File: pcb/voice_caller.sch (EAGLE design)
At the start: 44 parts, among them IC1 PRO_MICRO, IC2 LM386M-1, IC3 78L12SMD, K1 TQ2SA-L2-5V, U1 25F32006WSOI

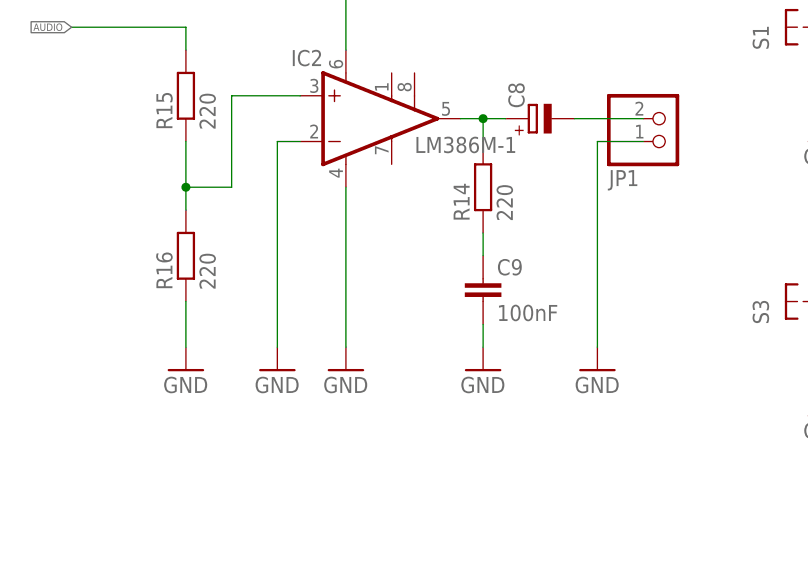
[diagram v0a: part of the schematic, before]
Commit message: Bypass capacitor added for LM386.
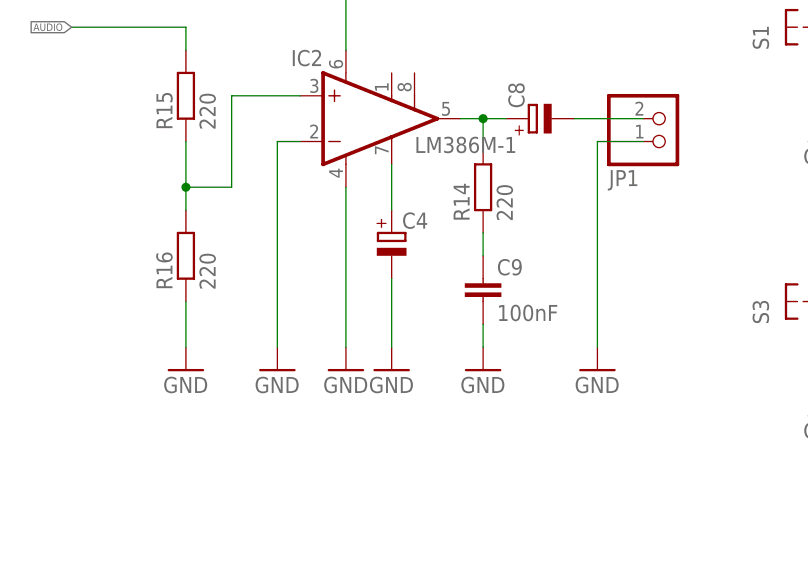
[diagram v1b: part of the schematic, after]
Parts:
- added C4: (no value), rcl:CPOL-EUE2.5-6
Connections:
- new net N$7: C4.+, IC2.BYPASS
- net GND: now also C4.-
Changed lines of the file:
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@@
 <part name="R16" library="rcl" deviceset="R-EU_" device="M1206" value="220"/>
 <part name="C11" library="rcl" deviceset="CPOL-EU" device="E2.5-6"/>
+<part name="GND26" library="supply1" deviceset="GND" device=""/>
+<part name="C4" library="rcl" deviceset="CPOL-EU" device="E2.5-6"/>
 </parts>
 <sheets>
@@
 <instance part="R16" gate="G$1" x="-91.44" y="104.14" rot="R90"/>
 <instance part="C11" gate="G$1" x="73.66" y="109.22" rot="R90"/>
+<instance part="GND26" gate="1" x="-68.58" y="91.44"/>
+<instance part="C4" gate="G$1" x="-68.58" y="106.68"/>
 </instances>
 <busses>
@@
 <pinref part="R16" gate="G$1" pin="1"/>
 </segment>
+<segment>
+<pinref part="GND26" gate="1" pin="GND"/>
+<pinref part="C4" gate="G$1" pin="-"/>
+<wire x1="-68.58" y1="93.98" x2="-68.58" y2="101.6" width="0.1524" layer="91"/>
+</segment>
 </net>
 <net name="MOSI" class="0">
@@
 </segment>
 </net>
+<net name="N$7" class="0">
+<segment>
+<pinref part="C4" gate="G$1" pin="+"/>
+<pinref part="IC2" gate="G$1" pin="BYPASS"/>
+<wire x1="-68.58" y1="109.22" x2="-68.58" y2="114.3" width="0.1524" layer="91"/>
+</segment>
+</net>

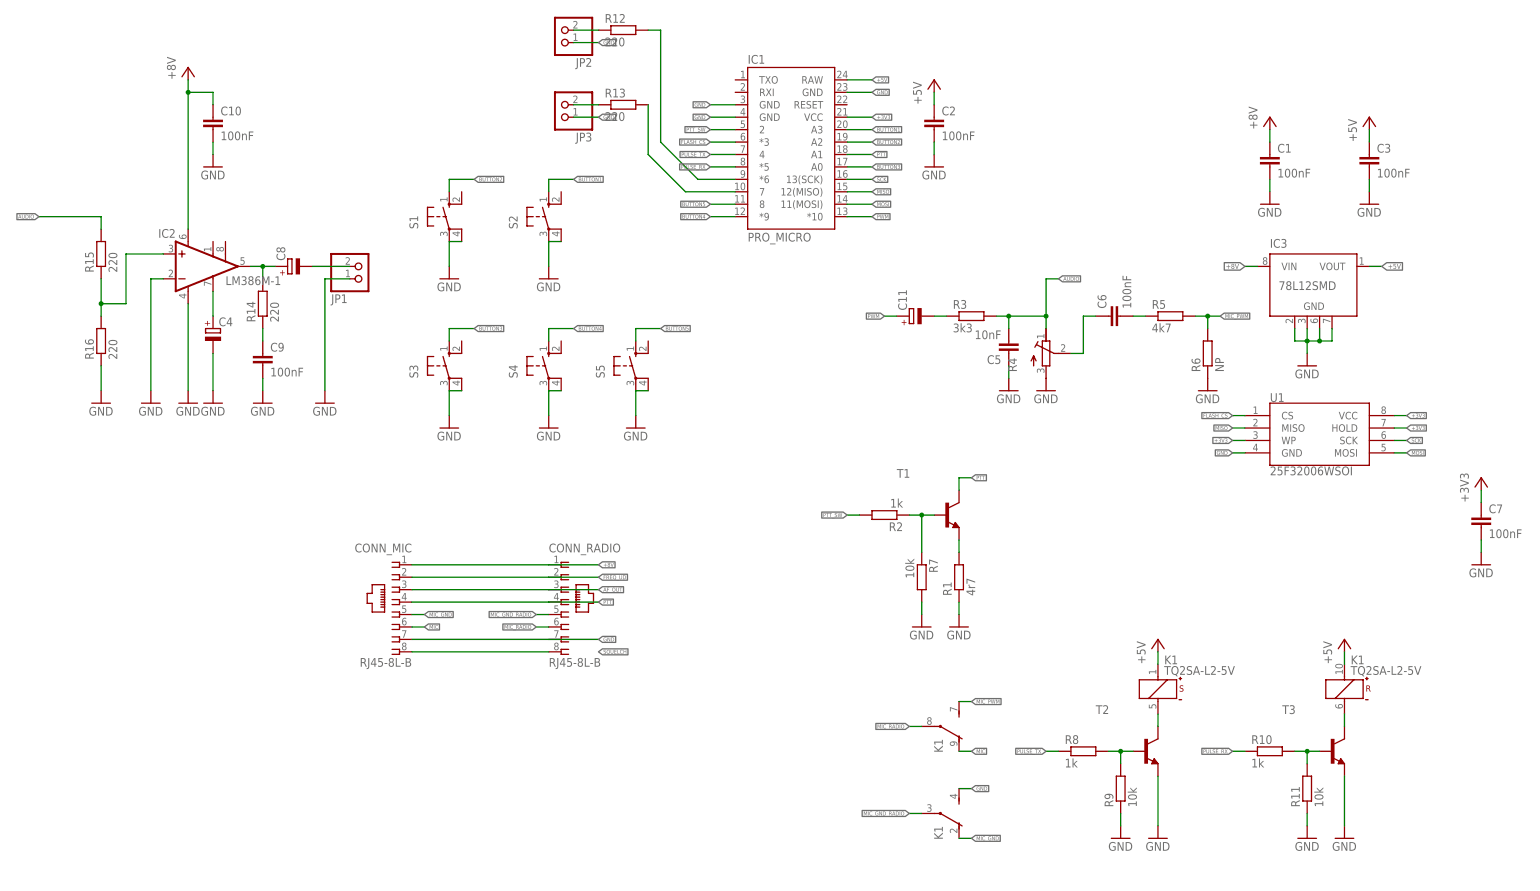
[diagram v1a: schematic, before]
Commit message: PTT sensing circuity added.
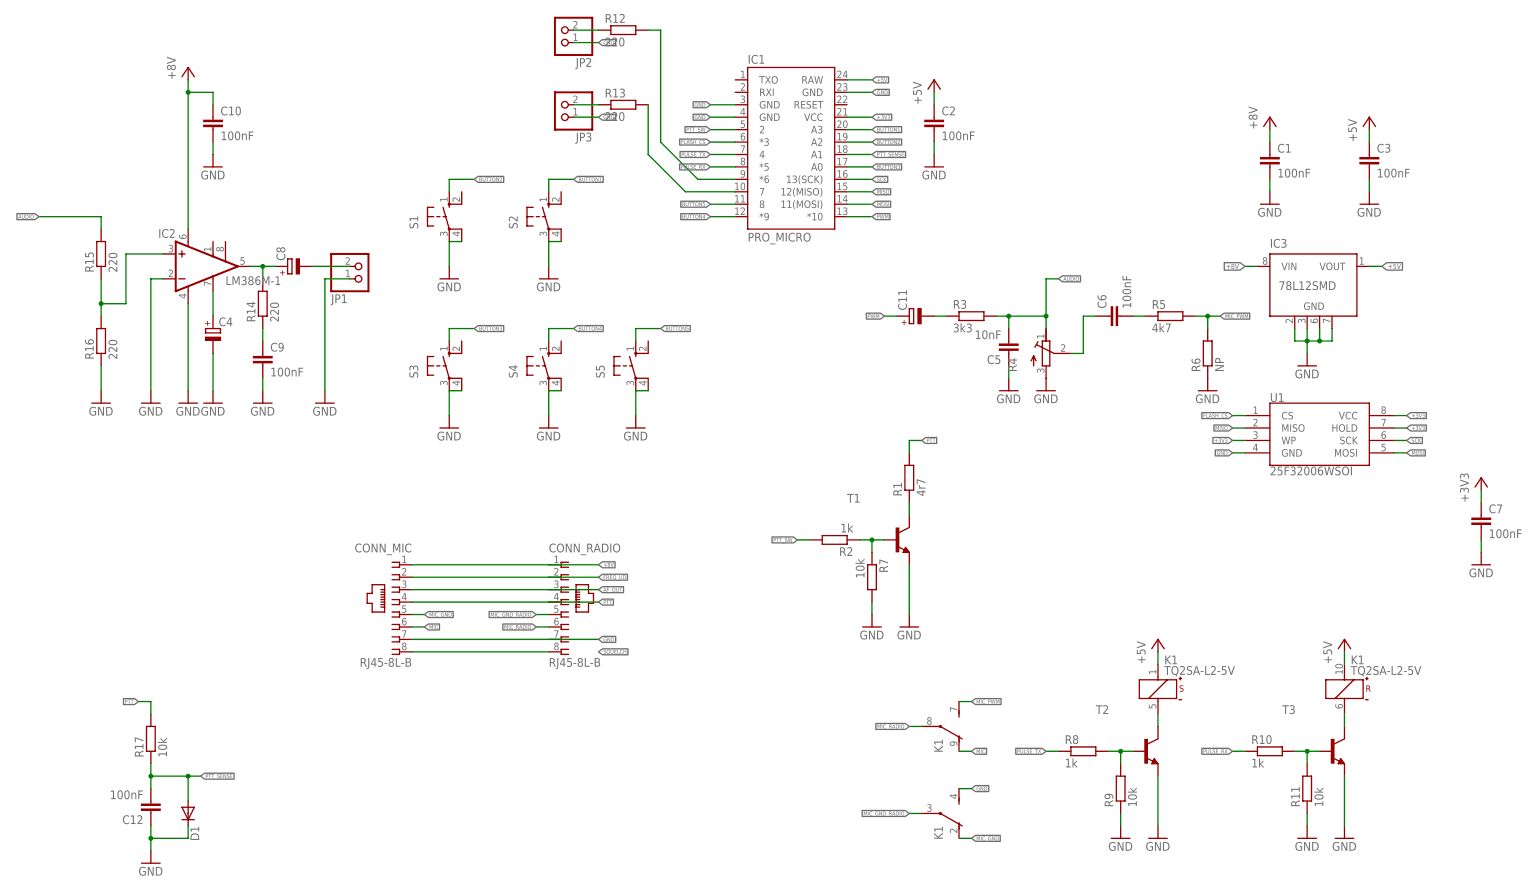
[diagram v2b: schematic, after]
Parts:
- added C12: 100nF, rcl:C-EUC1206K
- added D1: (no value), diode:DIODE-SOD80C
- added R17: 10k, rcl:R-EU_M1206
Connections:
- new net N$8: R1.1, T1.C
- net GND: now also C12.1, D1.C, T1.E; no longer R1.1
- net PTT: now also R1.2, R17.2; no longer IC1.A1, T1.C
- net PTT_SENSE: now also C12.2, D1.A, IC1.A1, R17.1; no longer R1.2, T1.E
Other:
- moved on the sheet: R1, R2, R7, T1
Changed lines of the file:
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@@
 <part name="GND26" library="supply1" deviceset="GND" device=""/>
 <part name="C4" library="rcl" deviceset="CPOL-EU" device="E2.5-6"/>
+<part name="R17" library="rcl" deviceset="R-EU_" device="M1206" value="10k"/>
+<part name="C12" library="rcl" deviceset="C-EU" device="C1206K" value="100nF"/>
+<part name="D1" library="diode" deviceset="DIODE-" device="SOD80C"/>
+<part name="GND27" library="supply1" deviceset="GND" device=""/>
 </parts>
 <sheets>
@@
 <instance part="S5" gate="1" x="17.78" y="99.06"/>
 <instance part="GND17" gate="1" x="17.78" y="86.36"/>
-<instance part="T1" gate="G$1" x="81.28" y="68.58"/>
-<instance part="R1" gate="G$1" x="83.82" y="55.88" rot="R90"/>
-<instance part="GND18" gate="1" x="83.82" y="45.72"/>
-<instance part="R2" gate="G$1" x="68.58" y="68.58" rot="R180"/>
-<instance part="R7" gate="G$1" x="76.2" y="55.88" rot="R270"/>
-<instance part="GND19" gate="1" x="76.2" y="45.72"/>
+<instance part="T1" gate="G$1" x="71.12" y="63.5"/>
+<instance part="R1" gate="G$1" x="73.66" y="76.2" rot="R90"/>
+<instance part="GND18" gate="1" x="73.66" y="45.72"/>
+<instance part="R2" gate="G$1" x="58.42" y="63.5" rot="R180"/>
+<instance part="R7" gate="G$1" x="66.04" y="55.88" rot="R270"/>
+<instance part="GND19" gate="1" x="66.04" y="45.72"/>
 <instance part="R12" gate="G$1" x="15.24" y="167.64"/>
 <instance part="R13" gate="G$1" x="15.24" y="152.4"/>
@@
 <instance part="GND26" gate="1" x="-68.58" y="91.44"/>
 <instance part="C4" gate="G$1" x="-68.58" y="106.68"/>
+<instance part="R17" gate="G$1" x="-81.28" y="22.86" rot="R90"/>
+<instance part="C12" gate="G$1" x="-81.28" y="7.62" rot="R180"/>
+<instance part="D1" gate="G$1" x="-73.66" y="7.62" rot="R270"/>
+<instance part="GND27" gate="1" x="-81.28" y="-2.54"/>
 </instances>
 <busses>
@@
 </segment>
 <segment>
-<pinref part="R1" gate="G$1" pin="1"/>
-<pinref part="GND18" gate="1" pin="GND"/>
-<wire x1="83.82" y1="48.26" x2="83.82" y2="50.8" width="0.1524" layer="91"/>
-</segment>
-<segment>
 <pinref part="R7" gate="G$1" pin="2"/>
 <pinref part="GND19" gate="1" pin="GND"/>
-<wire x1="76.2" y1="48.26" x2="76.2" y2="50.8" width="0.1524" layer="91"/>
+<wire x1="66.04" y1="48.26" x2="66.04" y2="50.8" width="0.1524" layer="91"/>
 </segment>
 <segment>
@@
 <pinref part="C4" gate="G$1" pin="-"/>
 <wire x1="-68.58" y1="93.98" x2="-68.58" y2="101.6" width="0.1524" layer="91"/>
+</segment>
+<segment>
+<pinref part="T1" gate="G$1" pin="E"/>
+<pinref part="GND18" gate="1" pin="GND"/>
+<wire x1="73.66" y1="58.42" x2="73.66" y2="48.26" width="0.1524" layer="91"/>
+</segment>
+<segment>
+<pinref part="C12" gate="G$1" pin="1"/>
+<wire x1="-81.28" y1="5.08" x2="-81.28" y2="2.54" width="0.1524" layer="91"/>
+<wire x1="-81.28" y1="2.54" x2="-73.66" y2="2.54" width="0.1524" layer="91"/>
+<pinref part="D1" gate="G$1" pin="C"/>
+<wire x1="-73.66" y1="2.54" x2="-73.66" y2="5.08" width="0.1524" layer="91"/>
+<pinref part="GND27" gate="1" pin="GND"/>
+<wire x1="-81.28" y1="0" x2="-81.28" y2="2.54" width="0.1524" layer="91"/>
+<junction x="-81.28" y="2.54"/>
 </segment>
 </net>
@@
 </segment>
 <segment>
-<pinref part="T1" gate="G$1" pin="C"/>
-<wire x1="83.82" y1="73.66" x2="83.82" y2="76.2" width="0.1524" layer="91"/>
-<wire x1="83.82" y1="76.2" x2="86.36" y2="76.2" width="0.1524" layer="91"/>
-<label x="86.36" y="76.2" size="0.8128" layer="95" xref="yes"/>
-</segment>
-<segment>
-<pinref part="IC1" gate="G$1" pin="A1"/>
-<wire x1="60.96" y1="142.24" x2="66.04" y2="142.24" width="0.1524" layer="91"/>
-<label x="66.04" y="142.24" size="0.8128" layer="95" xref="yes"/>
+<wire x1="73.66" y1="83.82" x2="76.2" y2="83.82" width="0.1524" layer="91"/>
+<label x="76.2" y="83.82" size="0.8128" layer="95" xref="yes"/>
+<pinref part="R1" gate="G$1" pin="2"/>
+<wire x1="73.66" y1="81.28" x2="73.66" y2="83.82" width="0.1524" layer="91"/>
+</segment>
+<segment>
+<pinref part="R17" gate="G$1" pin="2"/>
+<wire x1="-81.28" y1="27.94" x2="-81.28" y2="30.48" width="0.1524" layer="91"/>
+<wire x1="-81.28" y1="30.48" x2="-83.82" y2="30.48" width="0.1524" layer="91"/>
+<label x="-83.82" y="30.48" size="0.8128" layer="95" rot="R180" xref="yes"/>
 </segment>
 </net>
@@
 <net name="PTT_SENSE" class="0">
 <segment>
-<pinref part="T1" gate="G$1" pin="E"/>
-<pinref part="R1" gate="G$1" pin="2"/>
-<wire x1="83.82" y1="60.96" x2="83.82" y2="63.5" width="0.1524" layer="91"/>
+<pinref part="IC1" gate="G$1" pin="A1"/>
+<wire x1="60.96" y1="142.24" x2="66.04" y2="142.24" width="0.1524" layer="91"/>
+<label x="66.04" y="142.24" size="0.8128" layer="95" xref="yes"/>
+</segment>
+<segment>
+<pinref part="R17" gate="G$1" pin="1"/>
+<wire x1="-81.28" y1="17.78" x2="-81.28" y2="15.24" width="0.1524" layer="91"/>
+<pinref part="C12" gate="G$1" pin="2"/>
+<wire x1="-81.28" y1="15.24" x2="-81.28" y2="12.7" width="0.1524" layer="91"/>
+<wire x1="-81.28" y1="15.24" x2="-73.66" y2="15.24" width="0.1524" layer="91"/>
+<pinref part="D1" gate="G$1" pin="A"/>
+<wire x1="-73.66" y1="15.24" x2="-73.66" y2="10.16" width="0.1524" layer="91"/>
+<junction x="-81.28" y="15.24"/>
+<wire x1="-73.66" y1="15.24" x2="-71.12" y2="15.24" width="0.1524" layer="91"/>
+<junction x="-73.66" y="15.24"/>
+<label x="-71.12" y="15.24" size="0.8128" layer="95" xref="yes"/>
 </segment>
 </net>
@@
 <segment>
 <pinref part="R2" gate="G$1" pin="2"/>
-<wire x1="63.5" y1="68.58" x2="60.96" y2="68.58" width="0.1524" layer="91"/>
-<label x="60.96" y="68.58" size="0.8128" layer="95" rot="R180" xref="yes"/>
+<wire x1="53.34" y1="63.5" x2="50.8" y2="63.5" width="0.1524" layer="91"/>
+<label x="50.8" y="63.5" size="0.8128" layer="95" rot="R180" xref="yes"/>
 </segment>
 </net>
@@
 <pinref part="T1" gate="G$1" pin="B"/>
 <pinref part="R2" gate="G$1" pin="1"/>
-<wire x1="73.66" y1="68.58" x2="76.2" y2="68.58" width="0.1524" layer="91"/>
+<wire x1="63.5" y1="63.5" x2="66.04" y2="63.5" width="0.1524" layer="91"/>
 <pinref part="R7" gate="G$1" pin="1"/>
-<wire x1="76.2" y1="68.58" x2="78.74" y2="68.58" width="0.1524" layer="91"/>
-<wire x1="76.2" y1="60.96" x2="76.2" y2="68.58" width="0.1524" layer="91"/>
-<junction x="76.2" y="68.58"/>
+<wire x1="66.04" y1="63.5" x2="68.58" y2="63.5" width="0.1524" layer="91"/>
+<wire x1="66.04" y1="60.96" x2="66.04" y2="63.5" width="0.1524" layer="91"/>
+<junction x="66.04" y="63.5"/>
 </segment>
 </net>
@@
 </segment>
 </net>
+<net name="N$8" class="0">
+<segment>
+<pinref part="T1" gate="G$1" pin="C"/>
+<pinref part="R1" gate="G$1" pin="1"/>
+<wire x1="73.66" y1="71.12" x2="73.66" y2="68.58" width="0.1524" layer="91"/>
+</segment>
+</net>

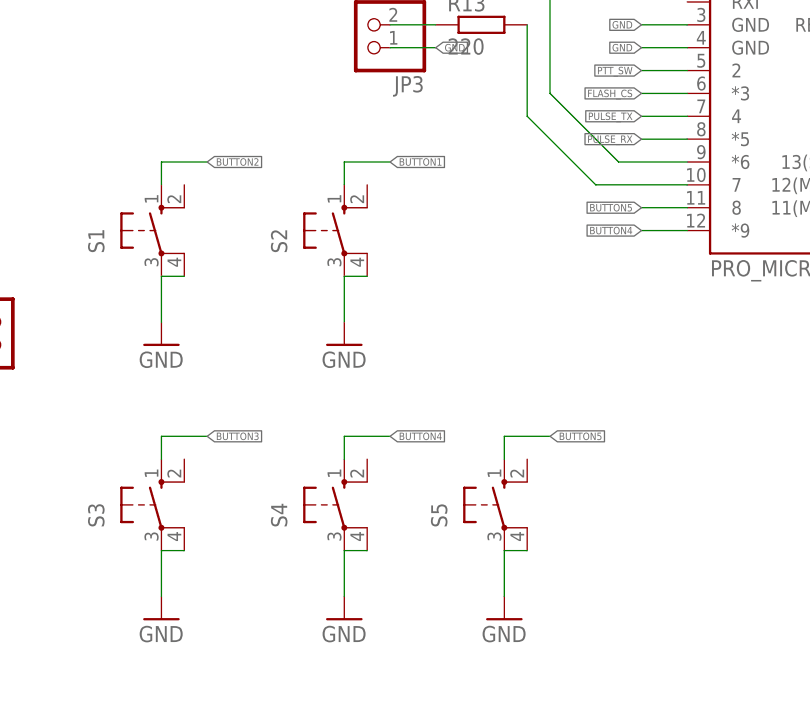
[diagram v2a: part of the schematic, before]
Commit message: Filter capacitors added to pushbuttons
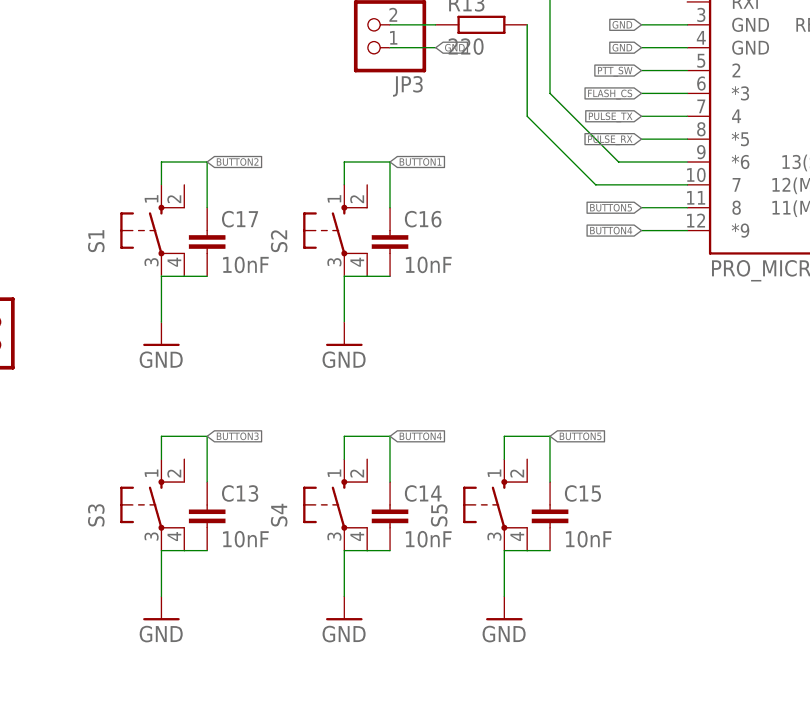
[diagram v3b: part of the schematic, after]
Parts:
- added C13, C14, C15, C16, C17: 10nF, rcl:C-EUC1206K
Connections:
- net BUTTON1: now also C16.1
- net BUTTON2: now also C17.1
- net BUTTON3: now also C13.1
- net BUTTON4: now also C14.1
- net BUTTON5: now also C15.1
- net GND: now also C13.2, C14.2, C15.2, C16.2, C17.2
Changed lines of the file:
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@@
 <part name="D1" library="diode" deviceset="DIODE-" device="SOD80C"/>
 <part name="GND27" library="supply1" deviceset="GND" device=""/>
+<part name="C13" library="rcl" deviceset="C-EU" device="C1206K" value="10nF"/>
+<part name="C14" library="rcl" deviceset="C-EU" device="C1206K" value="10nF"/>
+<part name="C15" library="rcl" deviceset="C-EU" device="C1206K" value="10nF"/>
+<part name="C16" library="rcl" deviceset="C-EU" device="C1206K" value="10nF"/>
+<part name="C17" library="rcl" deviceset="C-EU" device="C1206K" value="10nF"/>
 </parts>
 <sheets>
@@
 <instance part="D1" gate="G$1" x="-73.66" y="7.62" rot="R270"/>
 <instance part="GND27" gate="1" x="-81.28" y="-2.54"/>
+<instance part="C13" gate="G$1" x="-15.24" y="99.06"/>
+<instance part="C14" gate="G$1" x="5.08" y="99.06"/>
+<instance part="C15" gate="G$1" x="22.86" y="99.06"/>
+<instance part="C16" gate="G$1" x="5.08" y="129.54"/>
+<instance part="C17" gate="G$1" x="-15.24" y="129.54"/>
 </instances>
 <busses>
@@
 <pinref part="S1" gate="1" pin="P1"/>
 <wire x1="-20.32" y1="124.46" x2="-17.78" y2="124.46" width="0.1524" layer="91"/>
+<pinref part="C17" gate="G$1" pin="2"/>
+<wire x1="-15.24" y1="124.46" x2="-17.78" y2="124.46" width="0.1524" layer="91"/>
 </segment>
 <segment>
@@
 <pinref part="S2" gate="1" pin="P1"/>
 <wire x1="0" y1="124.46" x2="2.54" y2="124.46" width="0.1524" layer="91"/>
+<pinref part="C16" gate="G$1" pin="2"/>
+<wire x1="2.54" y1="124.46" x2="5.08" y2="124.46" width="0.1524" layer="91"/>
 </segment>
 <segment>
@@
 <pinref part="S3" gate="1" pin="P1"/>
 <wire x1="-20.32" y1="93.98" x2="-17.78" y2="93.98" width="0.1524" layer="91"/>
+<pinref part="C13" gate="G$1" pin="2"/>
+<wire x1="-17.78" y1="93.98" x2="-15.24" y2="93.98" width="0.1524" layer="91"/>
 </segment>
 <segment>
@@
 <pinref part="S4" gate="1" pin="P1"/>
 <wire x1="0" y1="93.98" x2="2.54" y2="93.98" width="0.1524" layer="91"/>
+<pinref part="C14" gate="G$1" pin="2"/>
+<wire x1="2.54" y1="93.98" x2="5.08" y2="93.98" width="0.1524" layer="91"/>
 </segment>
 <segment>
@@
 <pinref part="S5" gate="1" pin="P1"/>
 <wire x1="17.78" y1="93.98" x2="20.32" y2="93.98" width="0.1524" layer="91"/>
+<pinref part="C15" gate="G$1" pin="2"/>
+<wire x1="20.32" y1="93.98" x2="22.86" y2="93.98" width="0.1524" layer="91"/>
 </segment>
 <segment>
@@
 <wire x1="-20.32" y1="137.16" x2="-15.24" y2="137.16" width="0.1524" layer="91"/>
 <label x="-15.24" y="137.16" size="0.8128" layer="95" xref="yes"/>
+<pinref part="C17" gate="G$1" pin="1"/>
+<wire x1="-15.24" y1="132.08" x2="-15.24" y2="137.16" width="0.1524" layer="91"/>
 </segment>
 <segment>
@@
 <wire x1="0" y1="137.16" x2="5.08" y2="137.16" width="0.1524" layer="91"/>
 <label x="5.08" y="137.16" size="0.8128" layer="95" xref="yes"/>
+<pinref part="C16" gate="G$1" pin="1"/>
+<wire x1="5.08" y1="132.08" x2="5.08" y2="137.16" width="0.1524" layer="91"/>
 </segment>
 <segment>
@@
 <wire x1="-20.32" y1="106.68" x2="-15.24" y2="106.68" width="0.1524" layer="91"/>
 <label x="-15.24" y="106.68" size="0.8128" layer="95" xref="yes"/>
+<pinref part="C13" gate="G$1" pin="1"/>
+<wire x1="-15.24" y1="101.6" x2="-15.24" y2="106.68" width="0.1524" layer="91"/>
 </segment>
 </net>
@@
 <wire x1="17.78" y1="106.68" x2="22.86" y2="106.68" width="0.1524" layer="91"/>
 <label x="22.86" y="106.68" size="0.8128" layer="95" xref="yes"/>
+<pinref part="C15" gate="G$1" pin="1"/>
+<wire x1="22.86" y1="101.6" x2="22.86" y2="106.68" width="0.1524" layer="91"/>
 </segment>
 </net>
@@
 <wire x1="0" y1="106.68" x2="5.08" y2="106.68" width="0.1524" layer="91"/>
 <label x="5.08" y="106.68" size="0.8128" layer="95" xref="yes"/>
-</segment>
-</net>
+<pinref part="C14" gate="G$1" pin="1"/>
+<wire x1="5.08" y1="101.6" x2="5.08" y2="106.68" width="0.1524" layer="91"/>
+</segment>
+</net>
